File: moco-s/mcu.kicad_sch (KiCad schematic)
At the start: 13 parts, among them U3 STM32G431CBT6, Y1 32.768kHz, Y2 8MHz

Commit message: Update layout
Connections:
- net CAN_RX renamed CAN_~{INT}
- net CAN_TX renamed SPI_CAN_~{CS}
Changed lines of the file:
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@@
     (effects (font (size 1.27 1.27)) (justify left))
   )
-  (hierarchical_label "CAN_RX" (shape bidirectional) (at 173.99 130.81 0)
+  (hierarchical_label "CAN_~{INT}" (shape input) (at 173.99 130.81 0)
     (effects (font (size 1.27 1.27)) (justify left))
   )
@@
     (effects (font (size 1.27 1.27)) (justify left))
   )
-  (hierarchical_label "CAN_TX" (shape bidirectional) (at 140.97 120.65 180)
+  (hierarchical_label "SPI_CAN_~{CS}" (shape output) (at 140.97 120.65 180)
     (effects (font (size 1.27 1.27)) (justify right))
   )

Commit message: Comp MoCo-S
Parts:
- removed C37, C38: 12pF, Capacitor_SMD:C_0603_1608Metric, symbol Device:C_Small
- removed Y1: 32.768kHz, Crystal:Crystal_SMD_3215-2Pin_3.2x1.5mm, symbol Device:Crystal_Small
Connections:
- net GPIO_PB0 renamed USER_LED_1
- net GPIO_PB1 renamed USER_LED_2
- net GPIO_PB13 renamed SPI_DRIVER_~{CS}
- net GPIO_PB14 renamed SPI_SENSOR_~{CS}
- net ~{OCTW} renamed GPIO_PB11
- no-connect marks 0 -> 2
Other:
- note added: "I_{IO(PIN)} - Output current sunk by any I/O and control pin except FT_f: 20mA - Output current sunk by any FT_f pin: 20mA - Output current sourced by any I/O and control pin: 20mA"
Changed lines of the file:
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@@
   (junction (at 127 77.47) (diameter 0) (color 0 0 0 0)
   )
-  (junction (at 116.84 87.63) (diameter 0) (color 0 0 0 0)
-  )
   (junction (at 128.27 49.53) (diameter 0) (color 0 0 0 0)
   )
   (junction (at 120.65 49.53) (diameter 0) (color 0 0 0 0)
   )
-  (junction (at 102.87 90.17) (diameter 0) (color 0 0 0 0)
-  )
-  (junction (at 116.84 92.71) (diameter 0) (color 0 0 0 0)
-  )
   (junction (at 128.27 57.15) (diameter 0) (color 0 0 0 0)
   )
@@
   (junction (at 170.18 49.53) (diameter 0) (color 0 0 0 0)
   )
+  (no_connect (at 140.97 87.63))
+  (no_connect (at 140.97 92.71))
   (wire (pts (xy 113.03 82.55) (xy 118.11 82.55))
     (stroke (width 0) (type default) (color 0 0 0 0))
   )
-  (wire (pts (xy 116.84 92.71) (xy 140.97 92.71))
-    (stroke (width 0) (type default) (color 0 0 0 0))
-  )
   (wire (pts (xy 123.19 77.47) (xy 127 77.47))
     (stroke (width 0) (type default) (color 0 0 0 0))
@@
     (stroke (width 0) (type default) (color 0 0 0 0))
   )
-  (wire (pts (xy 102.87 87.63) (xy 102.87 90.17))
-    (stroke (width 0) (type default) (color 0 0 0 0))
-  )
   (wire (pts (xy 158.75 58.42) (xy 156.21 58.42))
     (stroke (width 0) (type default) (color 0 0 0 0))
   )
-  (wire (pts (xy 116.84 87.63) (xy 113.03 87.63))
-    (stroke (width 0) (type default) (color 0 0 0 0))
-  )
   (wire (pts (xy 157.48 142.24) (xy 158.75 142.24))
     (stroke (width 0) (type default) (color 0 0 0 0))
   )
-  (wire (pts (xy 116.84 92.71) (xy 113.03 92.71))
-    (stroke (width 0) (type default) (color 0 0 0 0))
-  )
   (wire (pts (xy 113.03 80.01) (xy 113.03 82.55))
     (stroke (width 0) (type default) (color 0 0 0 0))
@@
     (stroke (width 0) (type default) (color 0 0 0 0))
   )
-  (wire (pts (xy 102.87 92.71) (xy 107.95 92.71))
-    (stroke (width 0) (type default) (color 0 0 0 0))
-  )
   (wire (pts (xy 128.27 49.53) (xy 120.65 49.53))
     (stroke (width 0) (type default) (color 0 0 0 0))
@@
     (stroke (width 0) (type default) (color 0 0 0 0))
   )
-  (wire (pts (xy 102.87 87.63) (xy 107.95 87.63))
-    (stroke (width 0) (type default) (color 0 0 0 0))
-  )
-  (wire (pts (xy 102.87 90.17) (xy 102.87 92.71))
-    (stroke (width 0) (type default) (color 0 0 0 0))
-  )
   (wire (pts (xy 156.21 142.24) (xy 157.48 142.24))
     (stroke (width 0) (type default) (color 0 0 0 0))
@@
     (stroke (width 0) (type default) (color 0 0 0 0))
   )
-  (wire (pts (xy 101.6 90.17) (xy 102.87 90.17))
-    (stroke (width 0) (type default) (color 0 0 0 0))
-  )
   (wire (pts (xy 128.27 57.15) (xy 135.89 57.15))
     (stroke (width 0) (type default) (color 0 0 0 0))
   )
-  (wire (pts (xy 116.84 87.63) (xy 140.97 87.63))
-    (stroke (width 0) (type default) (color 0 0 0 0))
-  )
   (wire (pts (xy 153.67 142.24) (xy 156.21 142.24))
     (stroke (width 0) (type default) (color 0 0 0 0))
@@
     (stroke (width 0) (type default) (color 0 0 0 0))
   )
+  (text "I_{IO(PIN)}\n- Output current sunk by any I/O and control pin except FT_f: 20mA\n- Output current sunk by any FT_f pin: 20mA\n- Output current sourced by any I/O and control pin: 20mA"
+    (at 16.51 177.8 0)
+    (effects (font (size 1.27 1.27)) (justify left bottom))
+  )
   (text "PC13, PC14 and PC15 are supplied through the power switch. Since the switch only sinks a limited amount of current (3 mA),\nthe use of GPIOs PC13 to PC15 in output mode is limited:\n- The speed should not exceed 2 MHz with a maximum load of 30 pF\n- These GPIOs must not be used as current sources (for instance to drive an LED)."
-    (at 17.78 193.04 0)
+    (at 16.51 191.77 0)
     (effects (font (size 1.27 1.27)) (justify left bottom))
   )
-  (hierarchical_label "GPIO_PB13" (shape bidirectional) (at 140.97 130.81 180)
+  (hierarchical_label "SPI_DRIVER_~{CS}" (shape output) (at 140.97 130.81 180)
     (effects (font (size 1.27 1.27)) (justify right))
   )
@@
     (effects (font (size 1.27 1.27)) (justify left))
   )
-  (hierarchical_label "GPIO_PB0" (shape bidirectional) (at 140.97 99.06 180)
+  (hierarchical_label "USER_LED_1" (shape output) (at 140.97 99.06 180)
     (effects (font (size 1.27 1.27)) (justify right))
   )
@@
     (effects (font (size 1.27 1.27)) (justify left))
   )
-  (hierarchical_label "~{OCTW}" (shape input) (at 140.97 125.73 180)
-    (effects (font (size 1.27 1.27)) (justify right))
-  )
   (hierarchical_label "PWM_AH" (shape output) (at 173.99 123.19 0)
     (effects (font (size 1.27 1.27)) (justify left))
@@
     (effects (font (size 1.27 1.27)) (justify right))
   )
+  (hierarchical_label "GPIO_PB11" (shape bidirectional) (at 140.97 125.73 180)
+    (effects (font (size 1.27 1.27)) (justify right))
+  )
   (hierarchical_label "USART_RX" (shape input) (at 173.99 106.68 0)
     (effects (font (size 1.27 1.27)) (justify left))
@@
     (effects (font (size 1.27 1.27)) (justify left))
   )
-  (hierarchical_label "GPIO_PB14" (shape bidirectional) (at 140.97 133.35 180)
+  (hierarchical_label "SPI_SENSOR_~{CS}" (shape output) (at 140.97 133.35 180)
     (effects (font (size 1.27 1.27)) (justify right))
   )
@@
     (effects (font (size 1.27 1.27)) (justify right))
   )
-  (hierarchical_label "GPIO_PB1" (shape bidirectional) (at 140.97 101.6 180)
+  (hierarchical_label "USER_LED_2" (shape output) (at 140.97 101.6 180)
     (effects (font (size 1.27 1.27)) (justify right))
   )
@@
     (pin "1")
   )
-  (symbol (lib_id "Device:C_Small") (at 110.49 92.71 270) (unit 1)
-    (in_bom yes) (on_board yes)
-    (property "Reference" "C38" (id 0) (at 113.03 93.98 90))
-    (property "Value" "12pF" (id 1) (at 106.68 93.98 90))
-    (property "Footprint" "Capacitor_SMD:C_0603_1608Metric" (id 2) (at 110.49 92.71 0)
-      (effects (font (size 1.27 1.27)) hide)
-    )
-    (property "Datasheet" "~" (id 3) (at 110.49 92.71 0)
-      (effects (font (size 1.27 1.27)) hide)
-    )
-    (pin "1")
-    (pin "2")
-  )
   (symbol (lib_id "power:GND") (at 129.54 80.01 90) (unit 1)
     (in_bom yes) (on_board yes)
@@
     (pin "2")
   )
-  (symbol (lib_id "power:GND") (at 101.6 90.17 270) (unit 1)
-    (in_bom yes) (on_board yes)
-    (property "Reference" "#PWR075" (id 0) (at 95.25 90.17 0)
-      (effects (font (size 1.27 1.27)) hide)
-    )
-    (property "Value" "GND" (id 1) (at 99.06 90.17 90)
-      (effects (font (size 1.27 1.27)) (justify right))
-    )
-    (property "Footprint" "" (id 2) (at 101.6 90.17 0)
-      (effects (font (size 1.27 1.27)) hide)
-    )
-    (property "Datasheet" "" (id 3) (at 101.6 90.17 0)
-      (effects (font (size 1.27 1.27)) hide)
-    )
-    (pin "1")
-  )
-  (symbol (lib_id "Device:Crystal_Small") (at 116.84 90.17 90) (unit 1)
-    (in_bom yes) (on_board yes)
-    (property "Reference" "Y1" (id 0) (at 119.38 88.9 90)
-      (effects (font (size 1.27 1.27)) (justify right))
-    )
-    (property "Value" "32.768kHz" (id 1) (at 119.38 91.44 90)
-      (effects (font (size 1.27 1.27)) (justify right))
-    )
-    (property "Footprint" "Crystal:Crystal_SMD_3215-2Pin_3.2x1.5mm" (id 2) (at 116.84 90.17 0)
-      (effects (font (size 1.27 1.27)) hide)
-    )
-    (property "Datasheet" "~" (id 3) (at 116.84 90.17 0)
-      (effects (font (size 1.27 1.27)) hide)
-    )
-    (property "JLCPCB Part #" "C130253" (id 4) (at 116.84 90.17 0)
-      (effects (font (size 1.27 1.27)) hide)
-    )
-    (property "MFR.Part #" "ABS07-32.768KHZ-T" (id 5) (at 116.84 90.17 0)
-      (effects (font (size 1.27 1.27)) hide)
-    )
-    (pin "1")
-    (pin "2")
-  )
   (symbol (lib_id "power:VCC") (at 177.8 49.53 0) (unit 1)
     (in_bom yes) (on_board yes)
@@
   (symbol (lib_id "Device:Crystal_GND24_Small") (at 127 80.01 270) (unit 1)
     (in_bom yes) (on_board yes)
-    (property "Reference" "Y2" (id 0) (at 127 76.2 90)
-      (effects (font (size 1.27 1.27)) (justify left))
-    )
-    (property "Value" "8MHz" (id 1) (at 127 83.82 90)
+    (property "Reference" "Y2" (id 0) (at 128.27 76.2 90)
+      (effects (font (size 1.27 1.27)) (justify left))
+    )
+    (property "Value" "8MHz" (id 1) (at 128.27 83.82 90)
       (effects (font (size 1.27 1.27)) (justify left))
     )
@@
     (pin "4")
   )
-  (symbol (lib_id "Device:C_Small") (at 110.49 87.63 90) (unit 1)
-    (in_bom yes) (on_board yes)
-    (property "Reference" "C37" (id 0) (at 113.03 86.36 90))
-    (property "Value" "12pF" (id 1) (at 106.68 86.36 90))
-    (property "Footprint" "Capacitor_SMD:C_0603_1608Metric" (id 2) (at 110.49 87.63 0)
-      (effects (font (size 1.27 1.27)) hide)
-    )
-    (property "Datasheet" "~" (id 3) (at 110.49 87.63 0)
-      (effects (font (size 1.27 1.27)) hide)
-    )
-    (pin "1")
-    (pin "2")
-  )
 )

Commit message: Update ref
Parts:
- renumbered C39 to C36, C40 to C37, C41 to C38, C42 to C39, C43 to C40, C44 to C41, C45 to C42, C46 to C43, Y2 to Y1
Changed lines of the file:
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@@
   (symbol (lib_id "Device:C") (at 135.89 53.34 0) (unit 1)
     (in_bom yes) (on_board yes)
-    (property "Reference" "C43" (id 0) (at 135.89 50.8 0)
+    (property "Reference" "C40" (id 0) (at 135.89 50.8 0)
       (effects (font (size 1.27 1.27)) (justify left))
     )
@@
   (symbol (lib_id "power:VCC") (at 120.65 49.53 0) (unit 1)
     (in_bom yes) (on_board yes)
-    (property "Reference" "#PWR077" (id 0) (at 120.65 53.34 0)
+    (property "Reference" "#PWR058" (id 0) (at 120.65 53.34 0)
       (effects (font (size 1.27 1.27)) hide)
     )
@@
   (symbol (lib_id "Device:C_Small") (at 120.65 82.55 270) (unit 1)
     (in_bom yes) (on_board yes)
-    (property "Reference" "C41" (id 0) (at 123.19 83.82 90))
+    (property "Reference" "C38" (id 0) (at 123.19 83.82 90))
     (property "Value" "12pF" (id 1) (at 116.84 83.82 90))
     (property "Footprint" "Capacitor_SMD:C_0402_1005Metric" (id 2) (at 120.65 82.55 0)
@@
   (symbol (lib_id "power:GND") (at 177.8 57.15 0) (unit 1)
     (in_bom yes) (on_board yes)
-    (property "Reference" "#PWR082" (id 0) (at 177.8 63.5 0)
+    (property "Reference" "#PWR063" (id 0) (at 177.8 63.5 0)
       (effects (font (size 1.27 1.27)) hide)
     )
@@
   (symbol (lib_id "power:GND") (at 129.54 80.01 90) (unit 1)
     (in_bom yes) (on_board yes)
-    (property "Reference" "#PWR079" (id 0) (at 135.89 80.01 0)
+    (property "Reference" "#PWR060" (id 0) (at 135.89 80.01 0)
       (effects (font (size 1.27 1.27)) hide)
     )
@@
   (symbol (lib_id "Device:C") (at 128.27 53.34 0) (unit 1)
     (in_bom yes) (on_board yes)
-    (property "Reference" "C42" (id 0) (at 128.27 50.8 0)
+    (property "Reference" "C39" (id 0) (at 128.27 50.8 0)
       (effects (font (size 1.27 1.27)) (justify left))
     )
@@
   (symbol (lib_id "power:GND") (at 157.48 143.51 0) (unit 1)
     (in_bom yes) (on_board yes)
-    (property "Reference" "#PWR080" (id 0) (at 157.48 149.86 0)
+    (property "Reference" "#PWR061" (id 0) (at 157.48 149.86 0)
       (effects (font (size 1.27 1.27)) hide)
     )
@@
   (symbol (lib_id "Device:C") (at 143.51 53.34 0) (unit 1)
     (in_bom yes) (on_board yes)
-    (property "Reference" "C44" (id 0) (at 143.51 50.8 0)
+    (property "Reference" "C41" (id 0) (at 143.51 50.8 0)
       (effects (font (size 1.27 1.27)) (justify left))
     )
@@
   (symbol (lib_id "Device:C") (at 120.65 53.34 0) (unit 1)
     (in_bom yes) (on_board yes)
-    (property "Reference" "C39" (id 0) (at 120.65 50.8 0)
+    (property "Reference" "C36" (id 0) (at 120.65 50.8 0)
       (effects (font (size 1.27 1.27)) (justify left))
     )
@@
   (symbol (lib_id "Device:C_Small") (at 120.65 77.47 90) (unit 1)
     (in_bom yes) (on_board yes)
-    (property "Reference" "C40" (id 0) (at 123.19 76.2 90))
+    (property "Reference" "C37" (id 0) (at 123.19 76.2 90))
     (property "Value" "12pF" (id 1) (at 116.84 76.2 90))
     (property "Footprint" "Capacitor_SMD:C_0402_1005Metric" (id 2) (at 120.65 77.47 0)
@@
   (symbol (lib_id "Device:C") (at 170.18 53.34 0) (unit 1)
     (in_bom yes) (on_board yes)
-    (property "Reference" "C45" (id 0) (at 170.18 50.8 0)
+    (property "Reference" "C42" (id 0) (at 170.18 50.8 0)
       (effects (font (size 1.27 1.27)) (justify left))
     )
@@
   (symbol (lib_id "Device:C") (at 177.8 53.34 0) (unit 1)
     (in_bom yes) (on_board yes)
-    (property "Reference" "C46" (id 0) (at 177.8 50.8 0)
+    (property "Reference" "C43" (id 0) (at 177.8 50.8 0)
       (effects (font (size 1.27 1.27)) (justify left))
     )
@@
   (symbol (lib_id "power:VCC") (at 177.8 49.53 0) (unit 1)
     (in_bom yes) (on_board yes)
-    (property "Reference" "#PWR081" (id 0) (at 177.8 53.34 0)
+    (property "Reference" "#PWR062" (id 0) (at 177.8 53.34 0)
       (effects (font (size 1.27 1.27)) hide)
     )
@@
   (symbol (lib_id "power:GND") (at 120.65 57.15 0) (unit 1)
     (in_bom yes) (on_board yes)
-    (property "Reference" "#PWR078" (id 0) (at 120.65 63.5 0)
+    (property "Reference" "#PWR059" (id 0) (at 120.65 63.5 0)
       (effects (font (size 1.27 1.27)) hide)
     )
@@
   (symbol (lib_id "power:GND") (at 111.76 80.01 270) (unit 1)
     (in_bom yes) (on_board yes)
-    (property "Reference" "#PWR076" (id 0) (at 105.41 80.01 0)
+    (property "Reference" "#PWR057" (id 0) (at 105.41 80.01 0)
       (effects (font (size 1.27 1.27)) hide)
     )
@@
   (symbol (lib_id "Device:Crystal_GND24_Small") (at 127 80.01 270) (unit 1)
     (in_bom yes) (on_board yes)
-    (property "Reference" "Y2" (id 0) (at 128.27 76.2 90)
-      (effects (font (size 1.27 1.27)) (justify left))
-    )
+    (property "Reference" "Y1" (id 0) (at 128.27 76.2 90)
+      (effects (font (size 1.27 1.27)) (justify left))
+    )

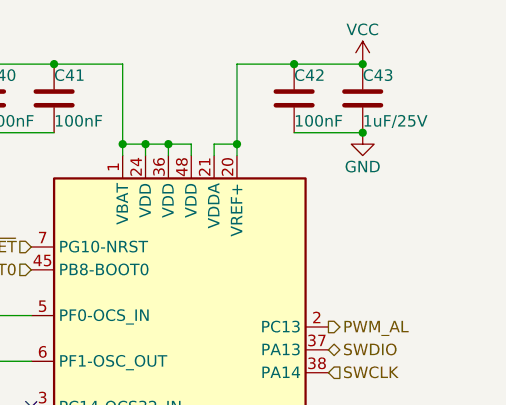
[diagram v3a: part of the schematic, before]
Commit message: Use kelvin connection for shunt resistance
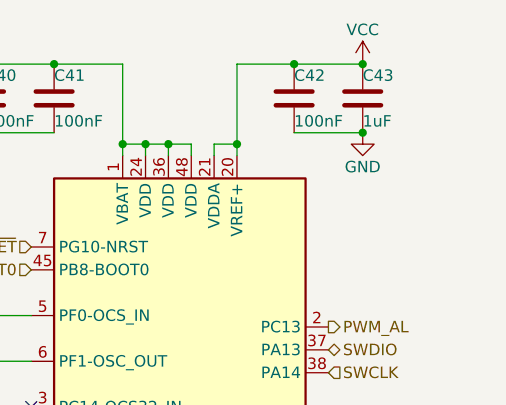
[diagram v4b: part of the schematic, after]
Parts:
- C37, C38: JLCPCB Part # (none) -> C1547; MFR.Part # (none) -> 0402CG120J500NT
- C43: value 1uF/25V -> 1uF; JLCPCB Part # (none) -> C52923; MFR.Part # (none) -> CL05A105KA5NQNC
- U3: JLCPCB Part # (none) -> C529355; MFR.Part # (none) -> STM32G431CBT6
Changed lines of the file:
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@@
+      (effects (font (size 1.27 1.27)) hide)
+    )
+    (property "JLCPCB Part #" "C1547" (id 4) (at 120.65 82.55 0)
+      (effects (font (size 1.27 1.27)) hide)
+    )
+    (property "MFR.Part #" "0402CG120J500NT" (id 5) (at 120.65 82.55 0)
       (effects (font (size 1.27 1.27)) hide)
     )
@@
     )
     (property "Datasheet" "" (id 3) (at 158.75 104.14 0)
+      (effects (font (size 1.27 1.27)) hide)
+    )
+    (property "JLCPCB Part #" "C529355" (id 4) (at 157.48 104.14 0)
+      (effects (font (size 1.27 1.27)) hide)
+    )
+    (property "MFR.Part #" "STM32G431CBT6" (id 5) (at 157.48 104.14 0)
       (effects (font (size 1.27 1.27)) hide)
     )
@@
       (effects (font (size 1.27 1.27)) hide)
     )
+    (property "JLCPCB Part #" "C1547" (id 4) (at 120.65 77.47 0)
+      (effects (font (size 1.27 1.27)) hide)
+    )
+    (property "MFR.Part #" "0402CG120J500NT" (id 5) (at 120.65 77.47 0)
+      (effects (font (size 1.27 1.27)) hide)
+    )
     (pin "1")
     (pin "2")
@@
       (effects (font (size 1.27 1.27)) (justify left))
     )
-    (property "Value" "1uF/25V" (id 1) (at 177.8 55.88 0)
+    (property "Value" "1uF" (id 1) (at 177.8 55.88 0)
       (effects (font (size 1.27 1.27)) (justify left))
     )
@@
       (effects (font (size 1.27 1.27)) hide)
     )
+    (property "JLCPCB Part #" "C52923" (id 4) (at 177.8 53.34 0)
+      (effects (font (size 1.27 1.27)) hide)
+    )
+    (property "MFR.Part #" "CL05A105KA5NQNC" (id 5) (at 177.8 53.34 0)
+      (effects (font (size 1.27 1.27)) hide)
+    )

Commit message: Replace some extended parts to basic parts
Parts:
- C36, C37, C38, C39, C40, C41, C42, C43: Basic Part (none) -> Y
- U3, Y1: Basic Part (none) -> N
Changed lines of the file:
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@@
+      (effects (font (size 1.27 1.27)) hide)
+    )
+    (property "Basic Part" "Y" (id 6) (at 135.89 53.34 0)
       (effects (font (size 1.27 1.27)) hide)
     )
@@
       (effects (font (size 1.27 1.27)) hide)
     )
+    (property "Basic Part" "Y" (id 6) (at 120.65 82.55 0)
+      (effects (font (size 1.27 1.27)) hide)
+    )
     (pin "1")
     (pin "2")
@@
     )
     (property "MFR.Part #" "STM32G431CBT6" (id 5) (at 157.48 104.14 0)
+      (effects (font (size 1.27 1.27)) hide)
+    )
+    (property "Basic Part" "N" (id 6) (at 157.48 104.14 0)
       (effects (font (size 1.27 1.27)) hide)
     )
@@
       (effects (font (size 1.27 1.27)) hide)
     )
+    (property "Basic Part" "Y" (id 6) (at 128.27 53.34 0)
+      (effects (font (size 1.27 1.27)) hide)
+    )
     (pin "1")
     (pin "2")
@@
       (effects (font (size 1.27 1.27)) hide)
     )
+    (property "Basic Part" "Y" (id 6) (at 143.51 53.34 0)
+      (effects (font (size 1.27 1.27)) hide)
+    )
     (pin "1")
     (pin "2")
@@
     )
     (property "MFR.Part #" "CL05B104KO5NNNC" (id 5) (at 120.65 53.34 0)
+      (effects (font (size 1.27 1.27)) hide)
+    )
+    (property "Basic Part" "Y" (id 6) (at 120.65 53.34 0)
       (effects (font (size 1.27 1.27)) hide)
     )
@@
       (effects (font (size 1.27 1.27)) hide)
     )
+    (property "Basic Part" "Y" (id 6) (at 120.65 77.47 0)
+      (effects (font (size 1.27 1.27)) hide)
+    )
     (pin "1")
     (pin "2")
@@
       (effects (font (size 1.27 1.27)) hide)
     )
+    (property "Basic Part" "Y" (id 6) (at 170.18 53.34 0)
+      (effects (font (size 1.27 1.27)) hide)
+    )
     (pin "1")
     (pin "2")
@@
     )
     (property "MFR.Part #" "CL05A105KA5NQNC" (id 5) (at 177.8 53.34 0)
+      (effects (font (size 1.27 1.27)) hide)
+    )
+    (property "Basic Part" "Y" (id 6) (at 177.8 53.34 0)
       (effects (font (size 1.27 1.27)) hide)
     )
@@
       (effects (font (size 1.27 1.27)) hide)
     )
+    (property "Basic Part" "N" (id 6) (at 127 80.01 0)
+      (effects (font (size 1.27 1.27)) hide)
+    )
